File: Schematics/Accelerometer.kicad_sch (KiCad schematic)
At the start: 3 parts, among them U9 H3LIS331DL

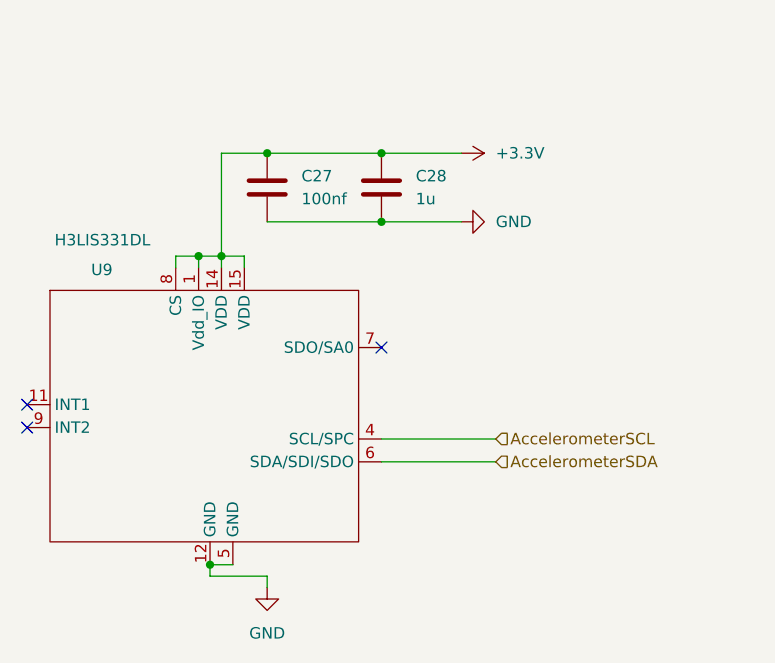
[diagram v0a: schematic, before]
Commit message: added aux pyro added reverse polarity protection re routed just need to clean up and check pin assignments
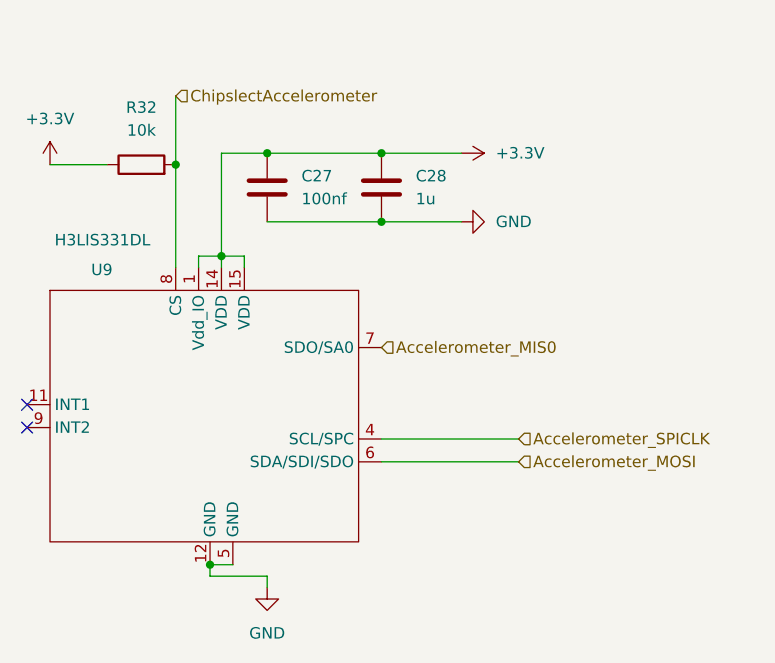
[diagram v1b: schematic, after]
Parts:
- added R32: 10k, Resistor_SMD:R_0805_2012Metric_Pad1.20x1.40mm_HandSolder, symbol Device:R
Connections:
- net +3.3V: now also R32.1; no longer U9.8 (CS)
- net Accelerometer_MIS0: now reaches U9.7 (SDO/SA0)
- net AccelerometerSCL renamed Accelerometer_SPICLK
- net AccelerometerSDA renamed Accelerometer_MOSI
- new net ChipslectAccelerometer: R32.2, U9.8 (CS)
- no-connect marks 3 -> 2

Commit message: added comments, awaiting review
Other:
- note added: "High g imu for liftoff data"
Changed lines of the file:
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@@
 	(generator_version "9.0")
 	(paper "A4")
+	(text "High g imu for liftoff data"
+		(exclude_from_sim no)
+		(at 156.718 65.278 0)
+		(effects
+			(font
+				(size 1.27 1.27)
+			)
+		)
+	)
 	(junction
 		(at 156.21 78.74)

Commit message: updated to KiCad 10.0, updated .gitignore
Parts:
- R32: LCSC C84376 -> C17414
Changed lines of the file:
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@@
 			)
 		)
-		(property "LCSC" "C84376"
+		(property "LCSC" "C17414"
 			(at 142.24 80.01 90)
 			(effects
